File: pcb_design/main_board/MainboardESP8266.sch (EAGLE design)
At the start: 67 parts, among them U1 ATECC108-SSHDA

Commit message: Added IMU and temperature sensor to main board
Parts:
- removed R12: 15k, SparkFun-Resistors:10KOHM1/10W1%(0603)0603
- removed R7: 10K, SparkFun-Resistors:10KOHM1/10W1%(0603)0603
- added C10, C11, C9: 0.1uF, SparkFun-Capacitors:0.1UF-25V(+80/-20%)(0603)
- added C12: 10nF, SparkFun-Capacitors:10NF/10000PF-50V-10%(0603)
- added C15: 10uF, SparkFun-Capacitors:10UF-6.3V-20%(0603)
- added D1, D2: (no value), SparkFun-LED:WS2812B
- added R18: 5k, SparkFun-Resistors:2.0KOHM1/10W5%(0603)
- added R19: (no value), SparkFun-Passives:RESISTOR-ARRAY0603-ARV
- added U2: TMP102, SparkFun-Sensors:TMP102
- added U3: LSM9DS1, LSM9DS1_temp:LSM9DS1
- R10, R11: value 2.0k -> 4.7k
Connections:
- removed net GPIO16/STEPUP_EN: ESP8266.GPIO16, MCP1640.EN, TP12.TP
- removed net GPIO4: ESP8266.GPIO4
- removed net N$4: ESP8266.GPIO12, R12.1, R7.1
- new net C1: C11.1, U3.C1
- new net CAP: C12.1, U3.CAP
- new net CS_A/G: R19B.1, U3.CS_A/G
- new net CS_M: R19A.1, U3.CS_M
- new net DEN_A/G: U3.DEN_A/G
- new net DRDY_M: U3.DRDY_M
- new net GPIO16/RGB: D1.DIN, ESP8266.GPIO16
- new net GPIO4/STEPUP_EN: ESP8266.GPIO4, MCP1640.EN, TP12.TP
- new net INT1_A/G: U3.INT1_A/G
- new net INT2_A/G: U3.INT2_A/G
- new net INT_M: U3.INT_M
- new net L1OUT: D1.DOUT, D2.DIN
- new net L2OUT: D2.DOUT
- new net N$10: R18.2, U2.ALERT
- new net RESET_AT: ESP8266.GPIO12, JP_RST.1
- new net SDO_A/G: R19D.1, U3.SDO_A/G
- new net SDO_M: R19C.1, U3.SDO_M
- net GND: now also C10.2, C11.2, C12.2, C15.2, C9.2, D1.VSS, D2.VSS, U2.ADD0, U2.GND, U3.GND, U3.RES; no longer R12.2
- net GPIO14/SCL: now also U2.SCL, U3.SCL/SPC
- net GPIO2/SDA: now also U2.SDA, U3.SDA/SDI/SDO
- net STAT: no longer R7.2
- net VCC: now also C10.1, C15.1, C9.1, D1.VDD, D2.VDD, R18.1, R19A.2, R19B.2, R19C.2, R19D.2, U2.VCC, U3.VDD, U3.VDDIO
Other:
- note added: "0 1"
- note added: "0x1C 0x1E"
- note added: "0x6A 0x6B"
- note added: "10102016: Added WS2812 RGB LEDs"
- note added: "11102016: Added LSM9DS1 IMU (interital measurement unit: gyroscope, accelerometer, magenetometer)"
- note added: "11102016: Added temperature sensor TMP102"
- note added: "13102016: Moved reset button to top layer"
- note added: "20102016: Added I2C address table"
- note added: "20102016: Added RST_AT to GPIO12 connection so that ESP8266 can reset motor board"
- note added: "20102016: Removed STAT - GPIO12 connection since STAT pin is not a reliable charge status indicator (mostly because the robot draws power during charging and therefore never really concludes charging)"
- note added: "AG Addr."
- note added: "Current sensor"
- note added: "Encryption chip"
- note added: "I2C Address Table (IMU)"
- note added: "I2C Address Table (overall)"
- note added: "I2C address: 0x03"
- note added: "I2C address: 0x45"
- note added: "I2C address: 0x60"
- note added: "I2C address: 0x68 (1001000)"
- note added: "IMU"
- note added: "Inertial Measurement Unit (IMU)"
- note added: "M Addr."
- note added: "Motor board"
- note added: "RGB LEDs"
- note added: "SDOM/AG"
- note added: "Set the SDO_AG and SDO_M to set the accel/gryo and mag I2C addresses:"
- note added: "Temperature Sensor"
- note added: "Temperature sensor"

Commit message: Fixed RGB LED setup on main board.
The RGB LEDs were connected to GPIO16, which on some versions
of the ESP8266 is connected to the RESET pin and can't be used
as general purpose pin after all. The RGB LEDs are now connected
to GPIO5 - the same pin as the status LED. Both types of LEDs can
be used together on the same pin.
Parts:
- R19: value (none) -> 10k
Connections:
- removed net GPIO16/RGB: D1.DIN, ESP8266.GPIO16
- removed net GPIO5: ESP8266.GPIO5, LED_USER.A
- new net GPIO5_LEDS: D1.DIN, ESP8266.GPIO5, LED_USER.A
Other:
- note added: "0"
- note added: "01112016: Moved RGB LEDs from GPIO16 to GPIO5 (since GPIO16 is tied to RESET and cannot be used). Note that WS2812 RGB LEDs and the regular indicator LED are both connected to GPIO5."
- note added: "0x1C"
- note added: "0x1E"
- note added: "0x6A"
- note added: "0x6B"
- note added: "1"
- note added: "TODO:"
- note removed: "0 1"
- note removed: "0x1C 0x1E"
- note removed: "0x6A 0x6B"

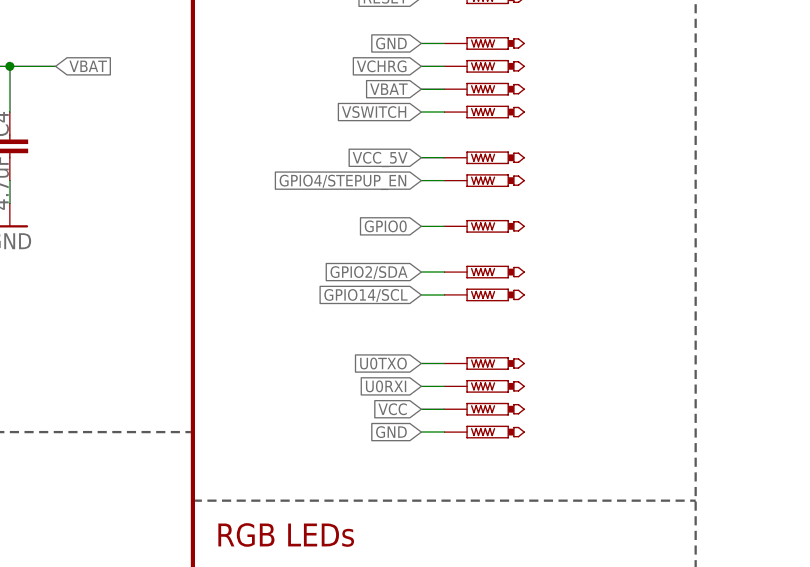
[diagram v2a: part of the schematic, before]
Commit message: Added test pin for GPIO5
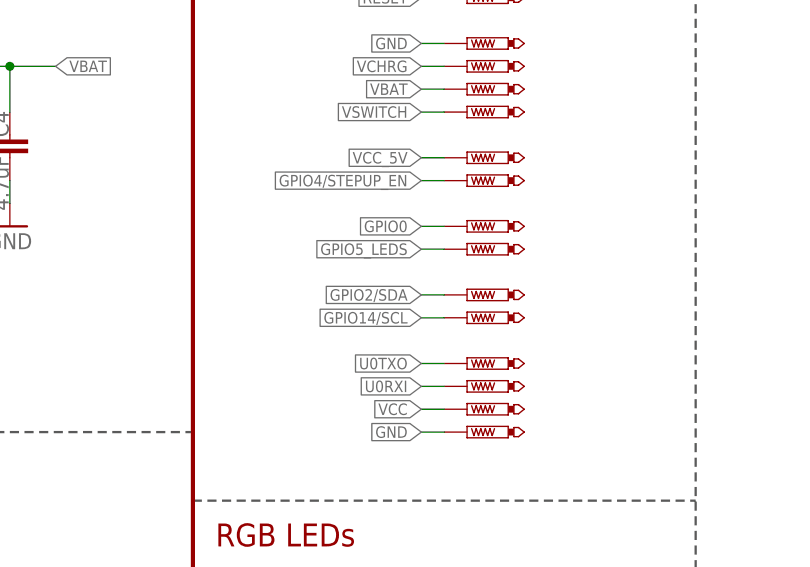
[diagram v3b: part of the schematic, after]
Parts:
- added TP15: PTR1B1,27, testpad:PTR1B1,27
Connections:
- net GPIO5_LEDS: now also TP15.TP
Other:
- note added: "09112016: Added GPIO5 test pin"
- note added: "TP15"
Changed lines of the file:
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@@
 <part name="SUPPLY2" library="SparkFun-Aesthetics" deviceset="VDD" device=""/>
 <part name="R19" library="SparkFun-Passives" deviceset="RESISTOR-ARRAY" device="0603-ARV" value="10k"/>
+<part name="TP15" library="testpad" deviceset="PTR1" device="B1,27"/>
 </parts>
 <sheets>
@@
 <text x="287.02" y="154.94" size="1.778" layer="98">TP12</text>
 <text x="287.02" y="149.86" size="1.778" layer="98">TP14</text>
-<text x="287.02" y="144.78" size="1.778" layer="98">TP6</text>
-<text x="287.02" y="142.24" size="1.778" layer="98">TP7</text>
+<text x="287.02" y="142.24" size="1.778" layer="98">TP6</text>
+<text x="287.02" y="139.7" size="1.778" layer="98">TP7</text>
 <text x="287.02" y="134.62" size="1.778" layer="98">TP2</text>
 <text x="287.02" y="132.08" size="1.778" layer="98">TP3</text>
@@
 <text x="327.406" y="11.43" size="2.54" layer="98" align="bottom-center">1</text>
 <text x="417.576" y="8.89" size="2.54" layer="94">Daniel Pickem</text>
+<text x="287.02" y="147.32" size="1.778" layer="98">TP15</text>
+<text x="309.88" y="132.08" size="1.778" layer="98" align="top-left">09112016: Added GPIO5 test pin</text>
 </plain>
 <instances>
@@
 <attribute name="TP_SIGNAL_NAME" x="281.94" y="158.75" size="1.778" layer="97" rot="R90"/>
 </instance>
-<instance part="TP6" gate="G$1" x="279.4" y="144.78" smashed="yes" rot="R90">
-<attribute name="TP_SIGNAL_NAME" x="281.94" y="146.05" size="1.778" layer="97" rot="R90"/>
-</instance>
-<instance part="TP7" gate="G$1" x="279.4" y="142.24" smashed="yes" rot="R90">
+<instance part="TP6" gate="G$1" x="279.4" y="142.24" smashed="yes" rot="R90">
 <attribute name="TP_SIGNAL_NAME" x="281.94" y="143.51" size="1.778" layer="97" rot="R90"/>
+</instance>
+<instance part="TP7" gate="G$1" x="279.4" y="139.7" smashed="yes" rot="R90">
+<attribute name="TP_SIGNAL_NAME" x="281.94" y="140.97" size="1.778" layer="97" rot="R90"/>
 </instance>
 <instance part="TP12" gate="G$1" x="279.4" y="154.94" smashed="yes" rot="R90">
@@
 <attribute name="NAME" x="427.7614" y="80.01" size="1.778" layer="95" rot="R90"/>
 <attribute name="VALUE" x="427.482" y="87.63" size="1.778" layer="96" rot="R90"/>
+</instance>
+<instance part="TP15" gate="G$1" x="279.4" y="147.32" smashed="yes" rot="R90">
+<attribute name="TP_SIGNAL_NAME" x="281.94" y="148.59" size="1.778" layer="97" rot="R90"/>
 </instance>
 </instances>
@@
 <segment>
 <pinref part="TP7" gate="G$1" pin="TP"/>
-<wire x1="276.86" y1="142.24" x2="274.32" y2="142.24" width="0.1524" layer="91"/>
-<label x="274.32" y="142.24" size="1.27" layer="95" rot="R180" xref="yes"/>
+<wire x1="276.86" y1="139.7" x2="274.32" y2="139.7" width="0.1524" layer="91"/>
+<label x="274.32" y="139.7" size="1.27" layer="95" rot="R180" xref="yes"/>
 </segment>
 <segment>
@@
 <segment>
 <pinref part="TP6" gate="G$1" pin="TP"/>
-<wire x1="276.86" y1="144.78" x2="274.32" y2="144.78" width="0.1524" layer="91"/>
-<label x="274.32" y="144.78" size="1.27" layer="95" rot="R180" xref="yes"/>
+<wire x1="276.86" y1="142.24" x2="274.32" y2="142.24" width="0.1524" layer="91"/>
+<label x="274.32" y="142.24" size="1.27" layer="95" rot="R180" xref="yes"/>
 </segment>
 <segment>
@@
 <label x="287.02" y="106.68" size="1.27" layer="95" xref="yes"/>
 </segment>
-</net>
+<segment>
+<pinref part="TP15" gate="G$1" pin="TP"/>
+<wire x1="276.86" y1="147.32" x2="274.32" y2="147.32" width="0.1524" layer="91"/>
+<label x="274.32" y="147.32" size="1.27" layer="95" rot="R180" xref="yes"/>
+</segment>
+</net>
